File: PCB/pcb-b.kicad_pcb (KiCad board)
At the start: 2 copper layers, 109.8 x 43.6 mm, 90 parts, among them K1 HK19F-DCxxV-SHC, Q1 BC817, Q10 BC817, Q11 TPCA8120,L1Q, Q12 BC817, Q13 TPCA8120,L1Q, Q14 BC817, Q15 BC817, Q17 BC327, Q18 BC327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

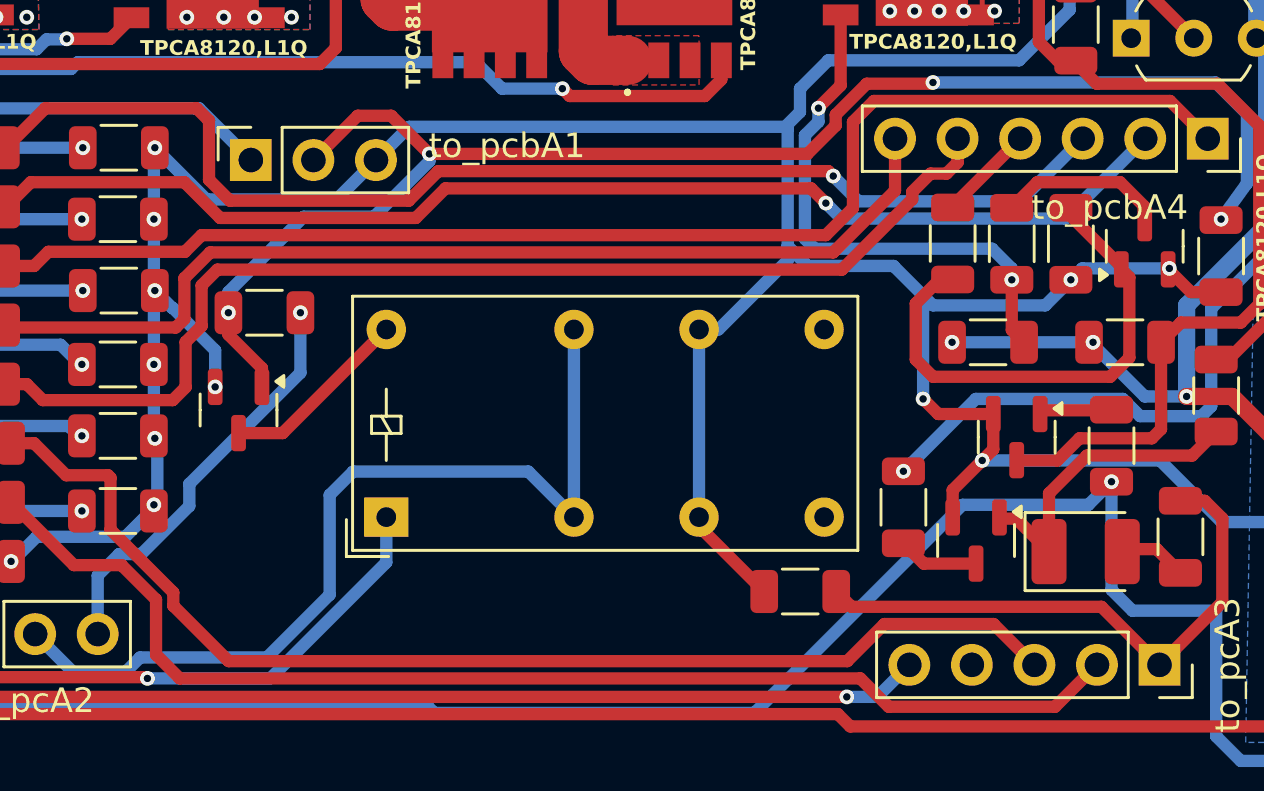
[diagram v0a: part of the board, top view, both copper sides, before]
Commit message: More stable solution for BJT driving
The BJT-817 device's sensibility is very high. If you are doing some test and you weld a wire to che i_PowerOFF pin, then you
can find the transistor's sturation while the wire is not connected.
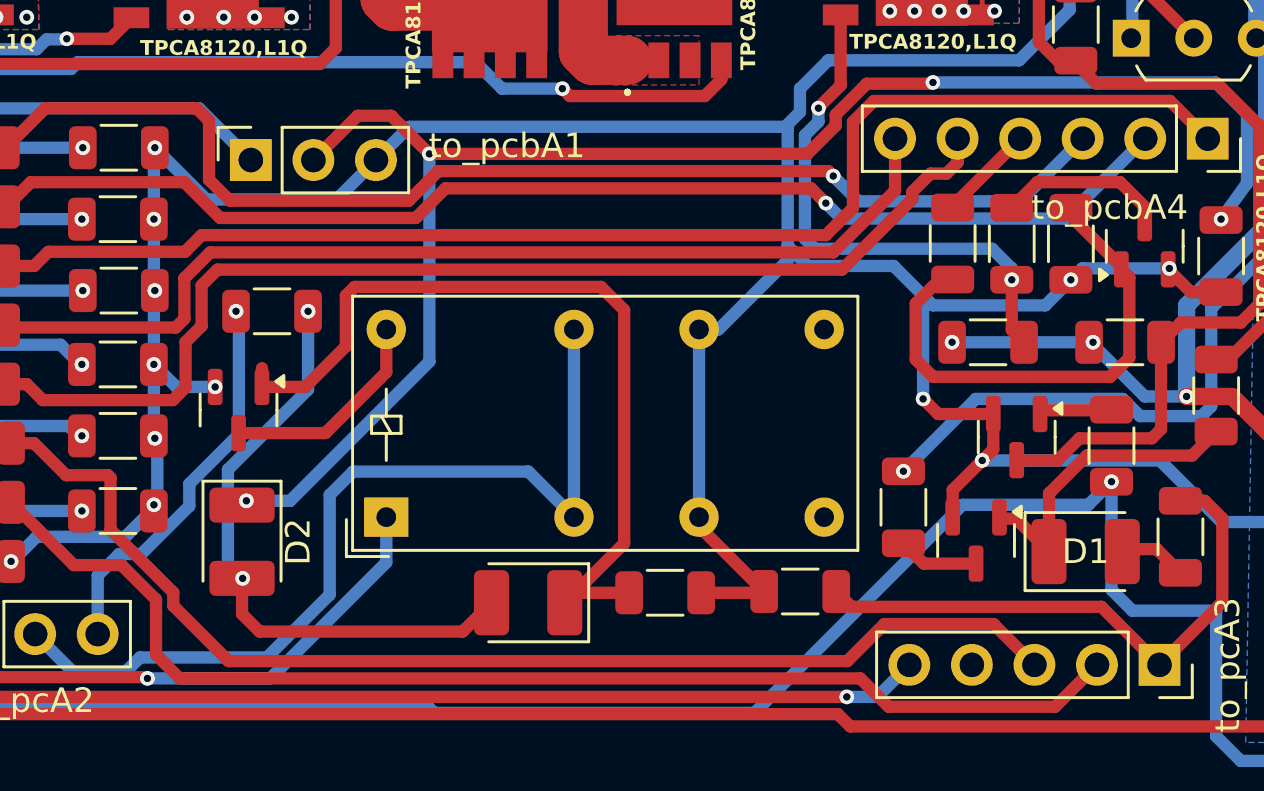
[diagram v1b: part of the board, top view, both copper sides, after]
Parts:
- added D2: D_Small, Diode_SMD:D_1210_3225Metric_Pad1.42x2.65mm_HandSolder, F.Cu at (143.4, 103.2)
- added D3: D_Small, Diode_SMD:D_1210_3225Metric_Pad1.42x2.65mm_HandSolder, F.Cu at (155.0, 105.6)
- added RA23: 100K, Resistor_SMD:R_1206_3216Metric, F.Cu at (160.6, 105.2)
- moved RA44 0.32 mm to (144.6, 93.8), turned to 0 degrees
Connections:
- Q12 pad 1: i_powerOFF -> Net-(D3-K)
- RA44 pad 2: i_powerOFF -> Net-(D2-A)
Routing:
- net Net-(D3-K): track 0.00 -> 34.4 mm
- net Net-(D2-A): track 0.00 -> 24.8 mm, vias 0 -> 2
- net i_powerOFF: track 61.0 -> 64.1 mm
- net Net-(Q12-C): track 7.74 -> 8.76 mm
- net o_engineON: track 17.0 -> 16.1 mm
- net GND: track 276.1 -> 276.6 mm

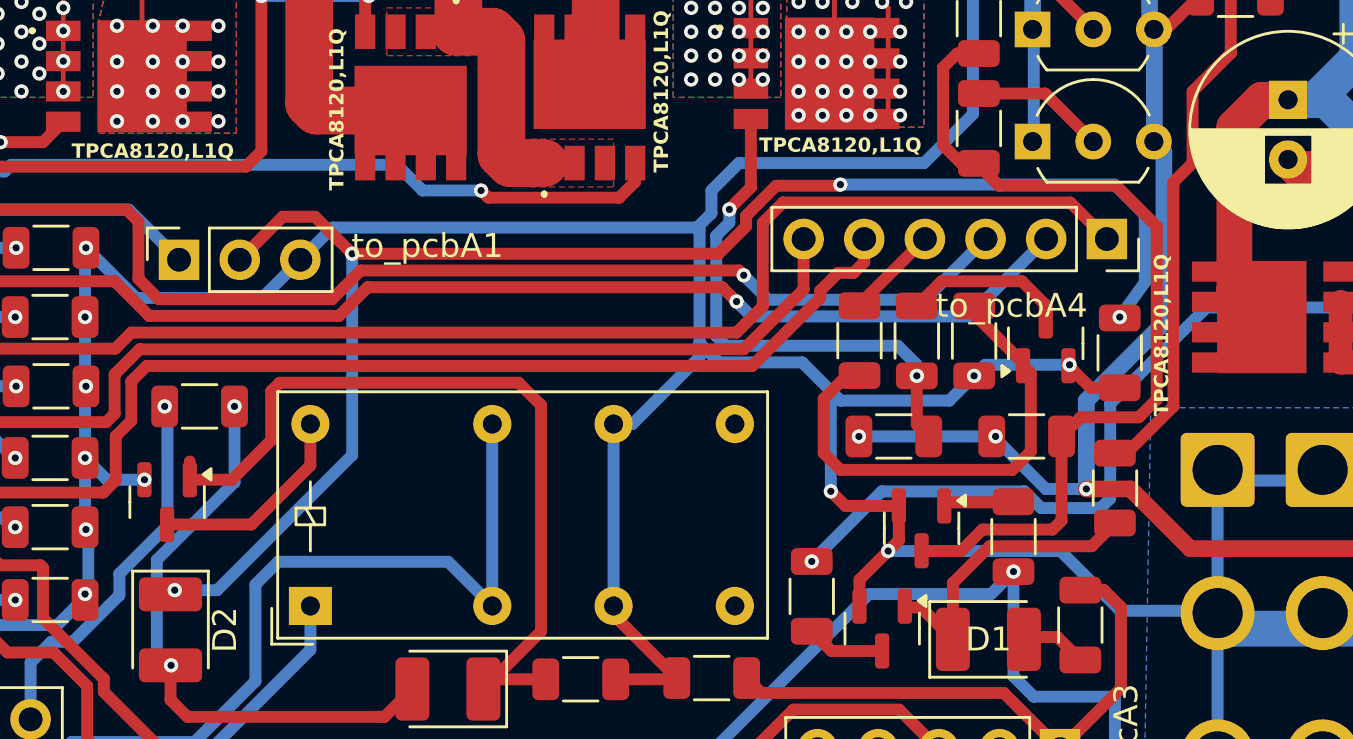
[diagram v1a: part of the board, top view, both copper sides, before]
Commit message: Unuseful wrong resistor deleted
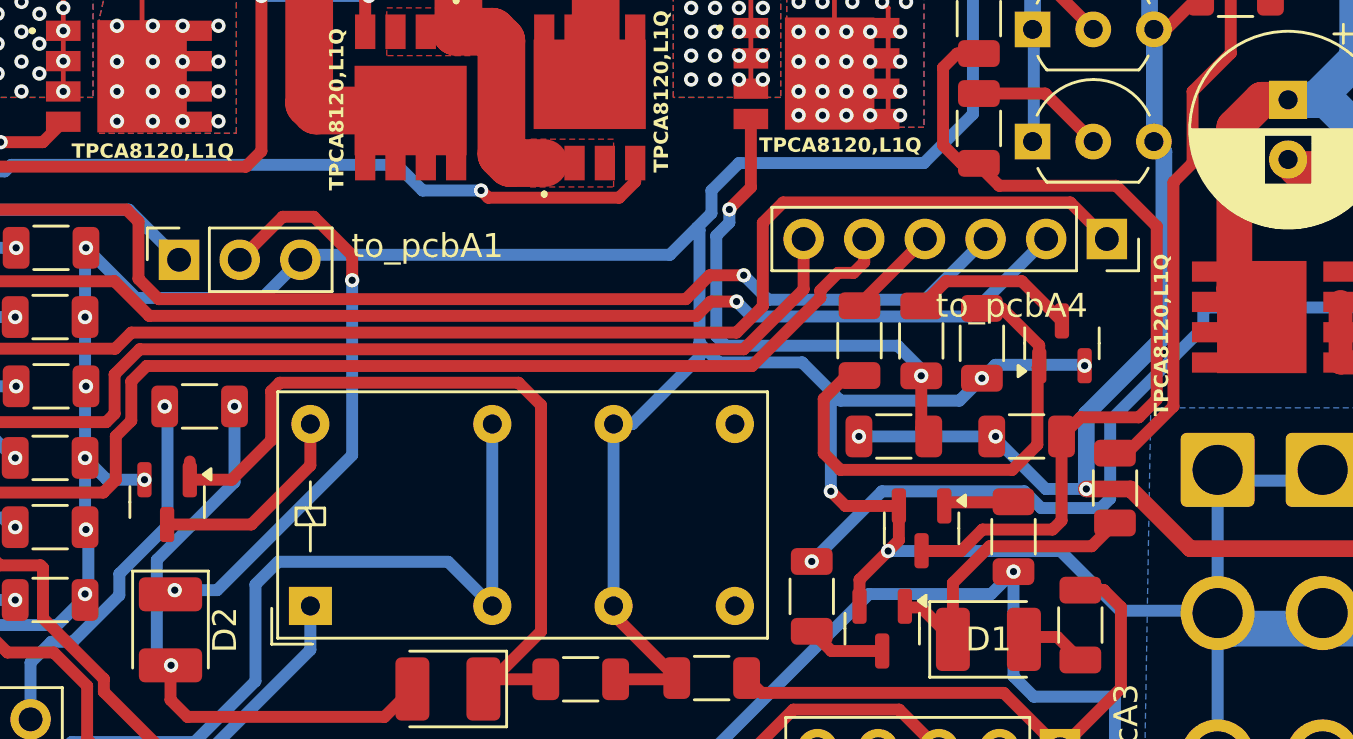
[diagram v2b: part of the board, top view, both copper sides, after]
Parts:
- removed RA41: 100K, Resistor_SMD:R_1206_3216Metric
- moved Q3 0.68 mm to (180.7, 91.2)
- moved RA32 0.34 mm to (177.4, 91.2)
- moved RA15 0.19 mm to (174.8, 91.0)
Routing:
- net i_powerOFF: track 64.1 -> 24.3 mm, vias 4 -> 2
- net GND: track 276.6 -> 274.6 mm
- net Net-(Q3-B): track 20.5 -> 21.1 mm

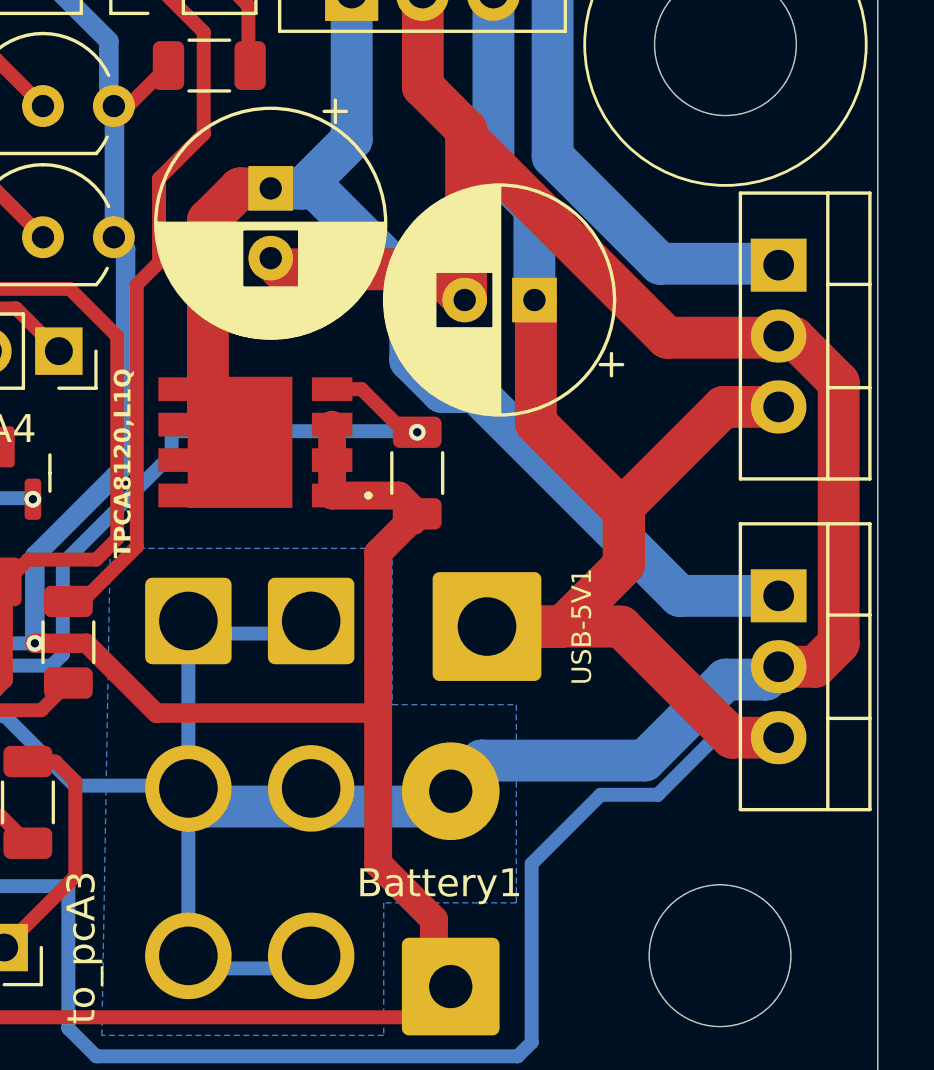
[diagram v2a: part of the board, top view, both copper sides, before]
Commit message: USB Power Supply connector fixed
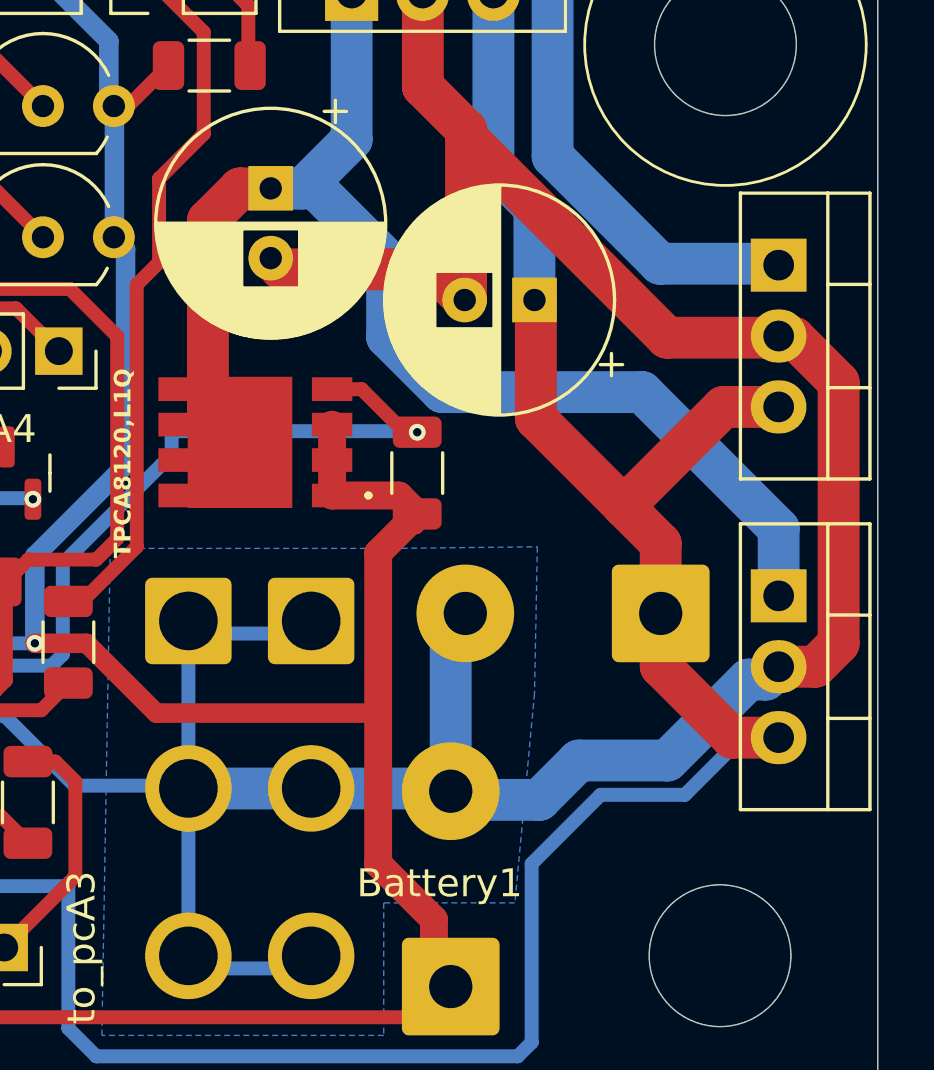
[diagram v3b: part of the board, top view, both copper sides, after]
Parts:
- USB-5V1: value Conn_01x01 -> Conn_01x02; footprint Connector_Wire:SolderWire-1.5sqmm_1x01_D1.7mm_OD3.9mm -> Connector_Wire:SolderWire-0.75sqmm_1x02_P7mm_D1.25mm_OD3.5mm
- moved USB-5V1 6.24 mm to (204.2, 96.2), turned to 180 degrees
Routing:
- net tempPower: track 187.6 -> 177.3 mm
- net GND: track 274.6 -> 281.0 mm
- net Net-(Q13-D_1): track 71.8 -> 73.2 mm

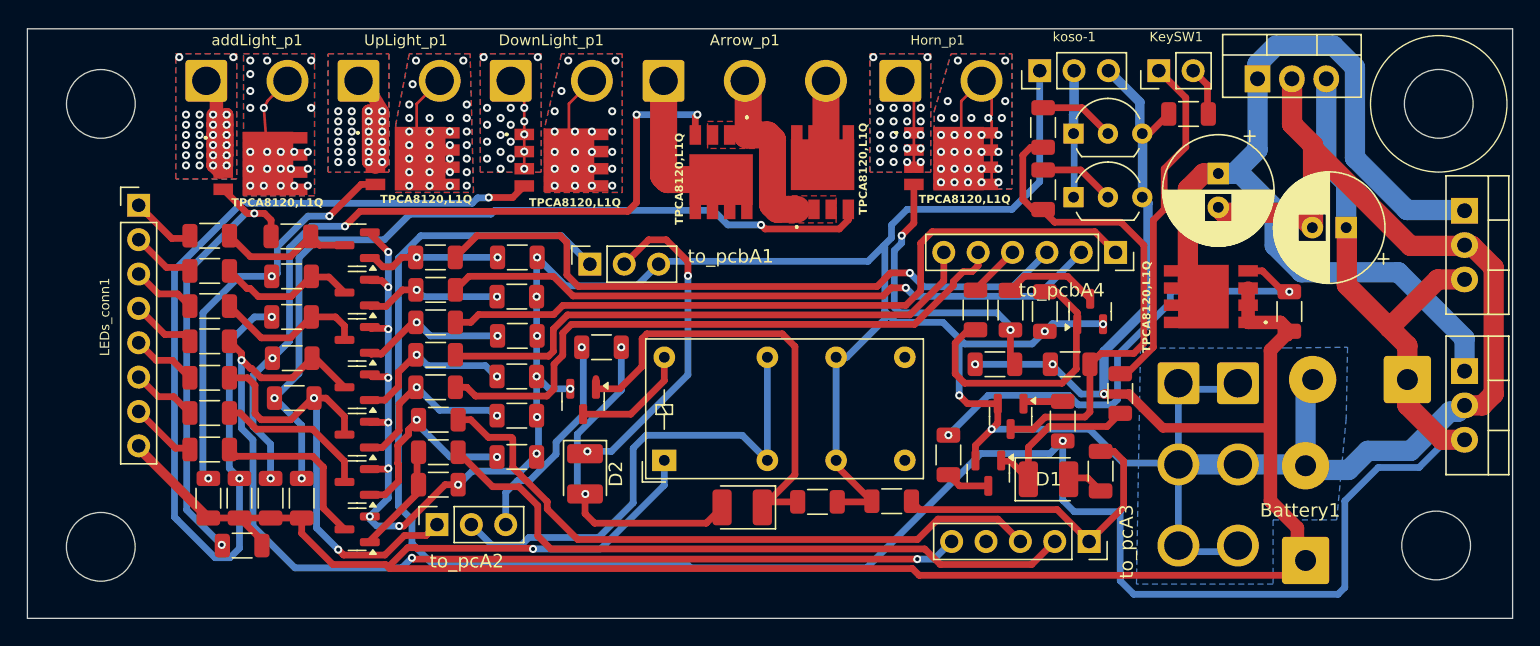
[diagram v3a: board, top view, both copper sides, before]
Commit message: Pin-header connectors adjustment
The main idea to mount the two pcb-A on the pcbB has been dropped, because the result is a too much chatic one and I realized that
wires welder on the top is a dangerous solution, they can create unwanted contacts and short-circuits... So, I choise to place the
two PCB beside. So, in order to get a more ordered and clean solution, I am using flat cables instead wires, and pin-header
connectors instead of welding them directly. I foung good connectors where every female-plug is blocked in its male-socket. But,
they are available just for even numbers of pins. For this reason, I have adjusted all the pin-header connectors and their
positions.
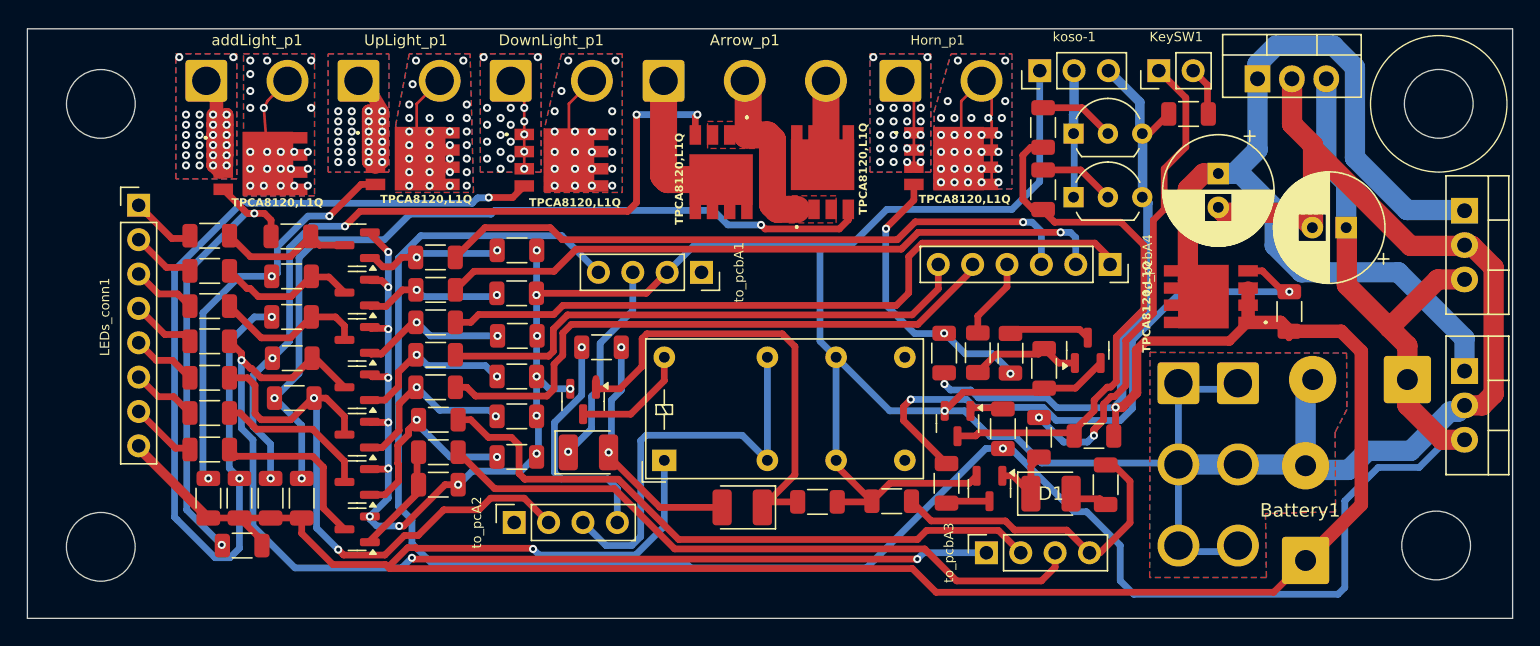
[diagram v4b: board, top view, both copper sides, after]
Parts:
- removed to_pcA3: Conn_01x05, Connector_PinSocket_2.54mm:PinSocket_1x05_P2.54mm_Vertical
- added to_pcbA3: Conn_01x04, Connector_PinSocket_2.54mm:PinSocket_1x04_P2.54mm_Vertical, F.Cu at (173.1, 109.0)
- to_pcA2, to_pcbA1: value Conn_01x03 -> Conn_01x04; footprint Connector_PinSocket_2.54mm:PinSocket_1x03_P2.54mm_Vertical -> Connector_PinSocket_2.54mm:PinSocket_1x04_P2.54mm_Vertical
- moved to_pcbA1 8.27 mm to (152.0, 88.3), turned to -90 degrees
- moved R4 6.82 mm to (176.9, 100.4)
- moved to_pcA2 5.71 mm to (138.2, 106.7)
- moved RA30 5.58 mm to (181.0, 100.3), turned to 0 degrees
- moved RA8 4.46 mm to (174.3, 99.8)
- moved RA32 4.20 mm to (177.3, 95.4)
- moved Q10 3.96 mm to (170.9, 99.4)
- moved RA42 3.84 mm to (169.9, 94.2), turned to -90 degrees
- moved RA15 3.19 mm to (174.8, 94.2)
- moved RA7 3.17 mm to (172.4, 94.2)
- moved Q3 2.88 mm to (180.6, 94.0)
- moved R3 2.10 mm to (170.1, 103.9)
- moved D2 1.61 mm to (143.6, 101.6), turned to 0 degrees
- moved Q9 1.13 mm to (173.3, 104.2)
- moved D1 1.08 mm to (177.8, 104.6)
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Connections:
- to_pcA2 pad 1: c_rightArrow -> unconnected-(to_pcA2-Pin_1-Pad1)
- to_pcA2 pad 2: c_engineOFF -> c_rightArrow
- to_pcA2 pad 3: o_engineON -> c_engineOFF
- to_pcbA1 pad 1: tempPower -> unconnected-(to_pcbA1-Pin_1-Pad1)
- to_pcbA1 pad 2: i_powerOFF -> GND
- to_pcbA1 pad 3: GND -> i_powerOFF
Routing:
- net +12V: track 197.2 -> 211.4 mm, vias 4 -> 3
- net Net-(Q3-B): track 21.1 -> 8.35 mm
- net Net-(KeySW1-Pin_1): track 25.5 -> 37.2 mm, vias 0 -> 2
- net c_rightArrow: track 33.9 -> 43.7 mm
- net Net-(Q13-G): track 36.3 -> 45.5 mm
- net i_powerOFF: track 24.3 -> 15.3 mm, vias 2 -> 1
- net Net-(D1-K): track 12.8 -> 5.61 mm
- net c_engineOFF: track 36.7 -> 30.3 mm
- net Net-(D2-A): track 24.8 -> 18.6 mm
- net tempPower: track 177.3 -> 173.7 mm
- net Net-(Q10-C): track 37.2 -> 40.6 mm
- net GND: track 281.0 -> 284.3 mm, vias 20 -> 17
- net c_leftArrow: track 77.8 -> 80.0 mm
- net o_horn: track 3.93 -> 5.96 mm
- net o_engineON: track 16.1 -> 17.7 mm
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- added copper zone on F.Cu, net GND

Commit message: o_NEUTRAL is connected directly to the led
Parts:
- removed Q20, Q3: BC817, Package_TO_SOT_SMD:SOT-23
- removed RA15: 33k, Resistor_SMD:R_1206_3216Metric
- removed RA17: 5K, Resistor_SMD:R_1206_3216Metric
- removed RA32, RA39: 100K, Resistor_SMD:R_1206_3216Metric
- RA42: value 10k -> 10K
- RA7: value 5K -> 33K
- moved Q21 3.07 mm to (126.6, 104.2)
- moved RA16 1.27 mm to (132.4, 100.3)
- moved RA40 1.16 mm to (132.4, 102.8)
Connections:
- net o_horn renamed c_horn
- RA6 pad 1: Net-(Q20-C) -> c_neutral
- RA7 pad 1: Net-(Q3-B) -> Net-(Q8-G)
- to_pcbA3 pad 2: o_neutral -> c_neutral
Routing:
- net c_neutral: track 0.00 -> 68.9 mm
- net o_neutral: track 47.4 -> 0.00 mm
- net GND: track 284.3 -> 261.0 mm, vias 17 -> 15
- net Net-(Q20-B): track 15.1 -> 0.00 mm, vias 2 -> 0
- net Net-(Q20-C): track 11.5 -> 0.00 mm
- net Net-(Q3-B): track 8.35 -> 0.00 mm
- net Net-(Q3-C): track 6.09 -> 0.00 mm
- net Net-(Q21-C): track 12.7 -> 9.67 mm
- net Net-(Q8-G): track 21.2 -> 19.4 mm, vias 3 -> 2
- net o_engineReady: track 49.6 -> 51.2 mm
- net Net-(Q21-B): track 8.23 -> 6.95 mm
- net Net-(Q19-B): track 13.3 -> 12.7 mm
